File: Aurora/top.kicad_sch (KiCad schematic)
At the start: 5 parts, among them J4 Screw_Terminal_01x08, J5 Screw_Terminal_01x08, U10 ADS1115IDGS, U11 ADS1115IDGS, U9 MCP23017T-E_SO

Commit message: reorganization
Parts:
- removed J4, J5: Screw_Terminal_01x08, footprints7:CONN_1715789_PXC, symbol Connector:Screw_Terminal_01x08
- removed U9: MCP23017T-E_SO, MCP23017T_E_SO:SOIC127P1030X265-28N, symbol MCP23017T-E_SO:MCP23017T-E_SO
- added C51: 0.33uF, Capacitor_SMD:C_1206_3216Metric, symbol Device:C_Small
- added C52: 100nF, Capacitor_SMD:C_1206_3216Metric, symbol Device:C_Small
- added J19, J20: TSW-104-27-G-D, TSW_104_27_G_D:SAMTEC_TSW-104-27-G-D, symbol TSW-104-27-G-D:TSW-104-27-G-D
- added J21: XT60-M, XT60-M:AMASS_XT60-M, symbol XT60-M:XT60-M
- added U12: L7805, L7805:TO255P1020X450X2000-3, symbol Regulator_Linear:L7805
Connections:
- net 5V: now also C52.1, J19.02, U12.3 (OUT)
- net ADC1_SCL: now also J19.04
- net ADC1_SDA: now also J19.03
- net ADC2_SCL: now also J19.06
- net ADC2_SDA: now also J19.05
- net GND: now also C51.2, C52.2, J19.08, J21.N (NEG), U12.2 (GND)
- new net 7.4V: C51.1, J20.01, J21.P (POS), U12.1 (IN)
- new net HDR_GPIO1: J20.02
- new net HDR_GPIO2: J20.03
- new net HDR_GPIO3: J20.04
- new net HDR_GPIO4: J20.05
- new net HDR_GPIO5: J20.06
- new net HDR_GPIO6: J20.07
- new net HDR_GPIO7: J20.08
- new net HDR_GPIO8: J19.01
- new net PYRO2: J19.07
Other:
- note added: "male Header Pins from bottom board"
- note removed: "16 I/O I2C Expander"

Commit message: Add files via upload
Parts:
- added C53, C58: 16PX10000MEFC16X31.5, CAP_PK/PZ_16X31P5_RUB, symbol 2025-11-18_06-04-35:16PX10000MEFC16X31.5
- added D1, D8: LED, LED_SMD:LED_Cree-PLCC4_5x5mm_CW, symbol Device:LED
- added D7: WS2812B-2020, LED_SMD:LED_WS2812B-2020_PLCC4_2.0x2.0mm, symbol LED:WS2812B-2020
- added J17: Screw_Terminal_01x02, footprints5:CONN_1729128_PXC, symbol Connector:Screw_Terminal_01x02
- added J18: Screw_Terminal_01x04, footprints6:CONN_1715747_PXC, symbol Connector:Screw_Terminal_01x04
- added J26, J27: Screw_Terminal_01x08, footprints7:CONN_1715789_PXC, symbol Connector:Screw_Terminal_01x08
- added J28, J29, J30, J31, J32, J37, J38: Screw_Terminal_01x03, symbol Connector:Screw_Terminal_01x03
- added J39: TSW-104-27-G-D, TSW_104_27_G_D:SAMTEC_TSW-104-27-G-D, symbol TSW-104-27-G-D:TSW-104-27-G-D
- added J40: XT60-M, XT60-M:AMASS_XT60-M, symbol XT60-M:XT60-M
- added R17: 10k, Resistor_SMD:R_1206_3216Metric, symbol Device:R_Small
- added R20: 20k, Resistor_SMD:R_1206_3216Metric, symbol Device:R_Small
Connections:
- net 5V: now also J27.1 (Pin_1), J27.2 (Pin_2), J27.3 (Pin_3), J27.4 (Pin_4), J27.5 (Pin_5), J27.6 (Pin_6), J27.7 (Pin_7), J27.8 (Pin_8)
- net 7.4V: now also C53.1, J28.2 (Pin_2), J29.2 (Pin_2), J30.2 (Pin_2), J31.2 (Pin_2), J32.2 (Pin_2), J37.2 (Pin_2), J38.2 (Pin_2), R17.1
- net ADC1_IN2: now also J17.1 (Pin_1)
- net ADC1_IN3: now also J17.2 (Pin_2)
- net ADC2_IN0: now also J18.1 (Pin_1)
- net ADC2_IN1: now also J18.2 (Pin_2)
- net ADC2_IN2: now also J18.3 (Pin_3)
- net ADC2_IN3: now also J18.4 (Pin_4)
- net GND: now also C53.2, C58.2, D1.1 (K), D7.2 (VSS), D8.1 (K), J26.1 (Pin_1), J26.2 (Pin_2), J26.3 (Pin_3), J26.4 (Pin_4), J26.5 (Pin_5), J26.6 (Pin_6), J26.7 (Pin_7), J26.8 (Pin_8), J28.3 (Pin_3), J29.3 (Pin_3), J30.3 (Pin_3), J31.3 (Pin_3), J32.3 (Pin_3), J37.3 (Pin_3), J38.3 (Pin_3), J40.N (NEG)
- net HDR_GPIO1: now also J39.01; no longer J20.02
- net HDR_GPIO2: now also J39.02; no longer J20.03
- net HDR_GPIO3: now also J39.03; no longer J20.04
- net HDR_GPIO4: now also J39.04; no longer J20.05
- net HDR_GPIO5: now also D7.3 (DIN), J39.05; no longer J20.06
- net ADC1_IN0 renamed PYRO1_CONT
- net ADC1_IN1 renamed PYRO2_CONT
- net HDR_GPIO6 renamed SERVO6
- net SERVO6: now also J37.1 (Pin_1), J38.1 (Pin_1)
- net HDR_GPIO7 renamed SERVO7
- net HDR_GPIO8 renamed PYRO1_GPIO
- net PYRO2 renamed PYRO2_GPIO
- new net: D1.2 (A), R17.2
- new net: D8.2 (A), R20.2
- new net 12V: J40.P (POS), R20.1
- new net 12v: C58.1
- new net 3V3: D7.4 (VDD)
- new net SERVO1: J20.02, J28.1 (Pin_1)
- new net SERVO2: J20.03, J29.1 (Pin_1)
- new net SERVO3: J20.04, J30.1 (Pin_1)
- new net SERVO4: J20.05, J31.1 (Pin_1)
- new net SERVO5: J20.06, J32.1 (Pin_1)
- new net SLN_1: J39.07
- new net SLN_2: J39.08
- new net SPKG: J39.06
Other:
- note added: "10,000uF"
- note added: "ADC"
- note added: "Add redundant mosfets for powering solenoid"
- note added: "Blue LED"
- note added: "Check works with 3.3v logic (may need 5v booster)"
- note added: "Green LED"
- note added: "MISC"
- note added: "PYRO"
- note added: "Peripherals from bottom"
- note added: "Power Top"
- note added: "Servos"
- note added: "Solenoid"
- note added: "Spark Plug"
- moved on the sheet: C51, C52, J19, J20, J21, U10, U11, U12

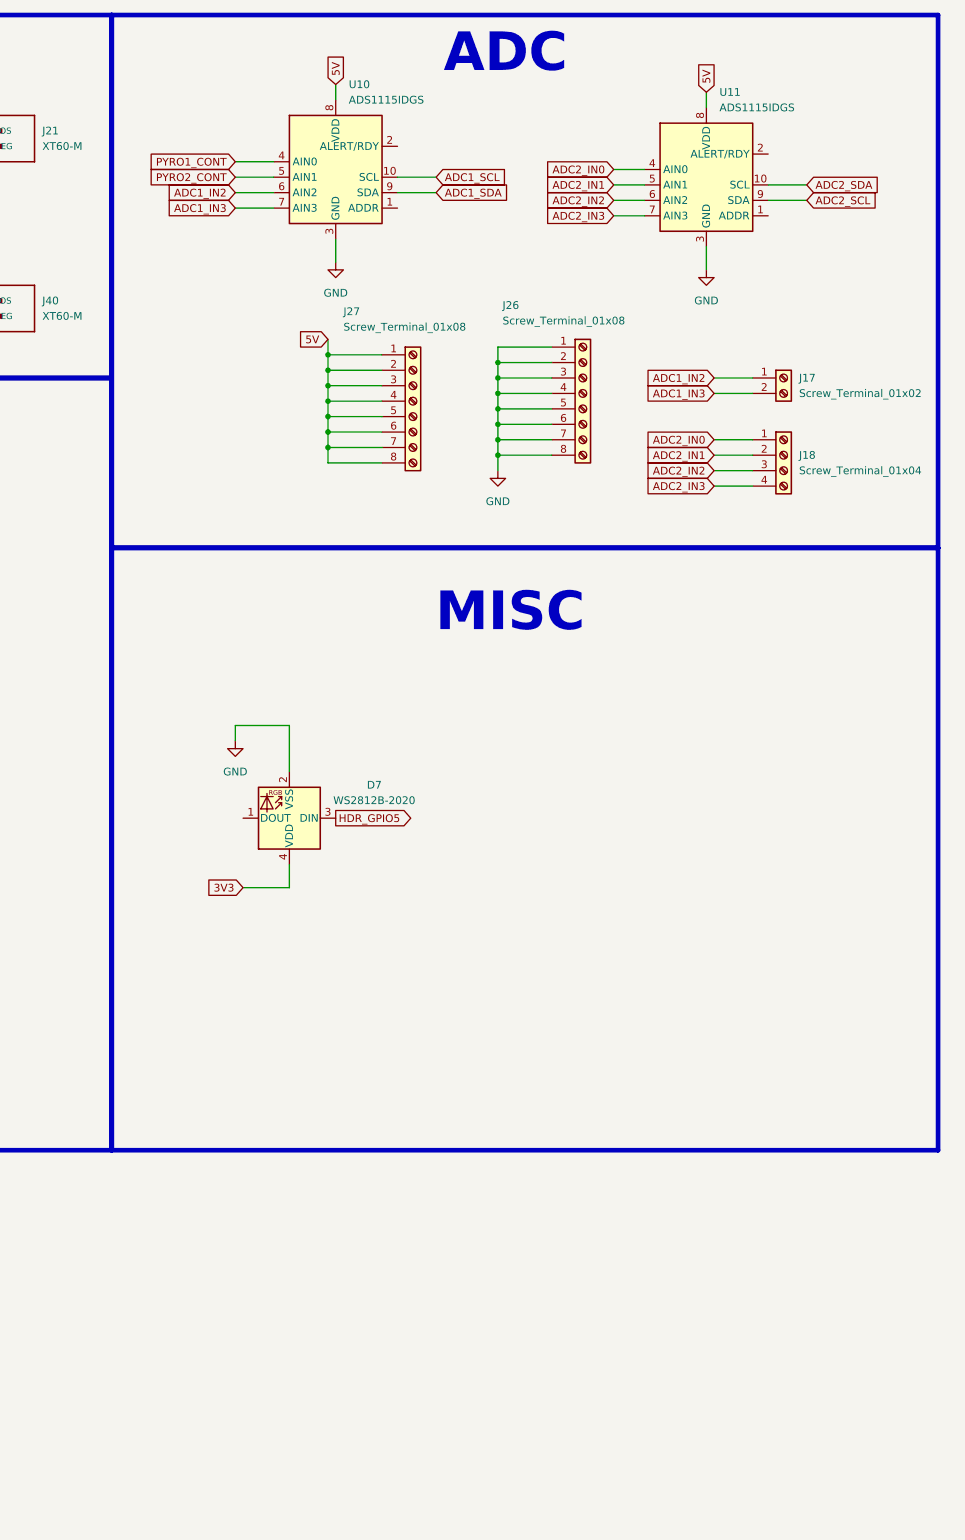
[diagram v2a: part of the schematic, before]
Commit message: 3rd ADC
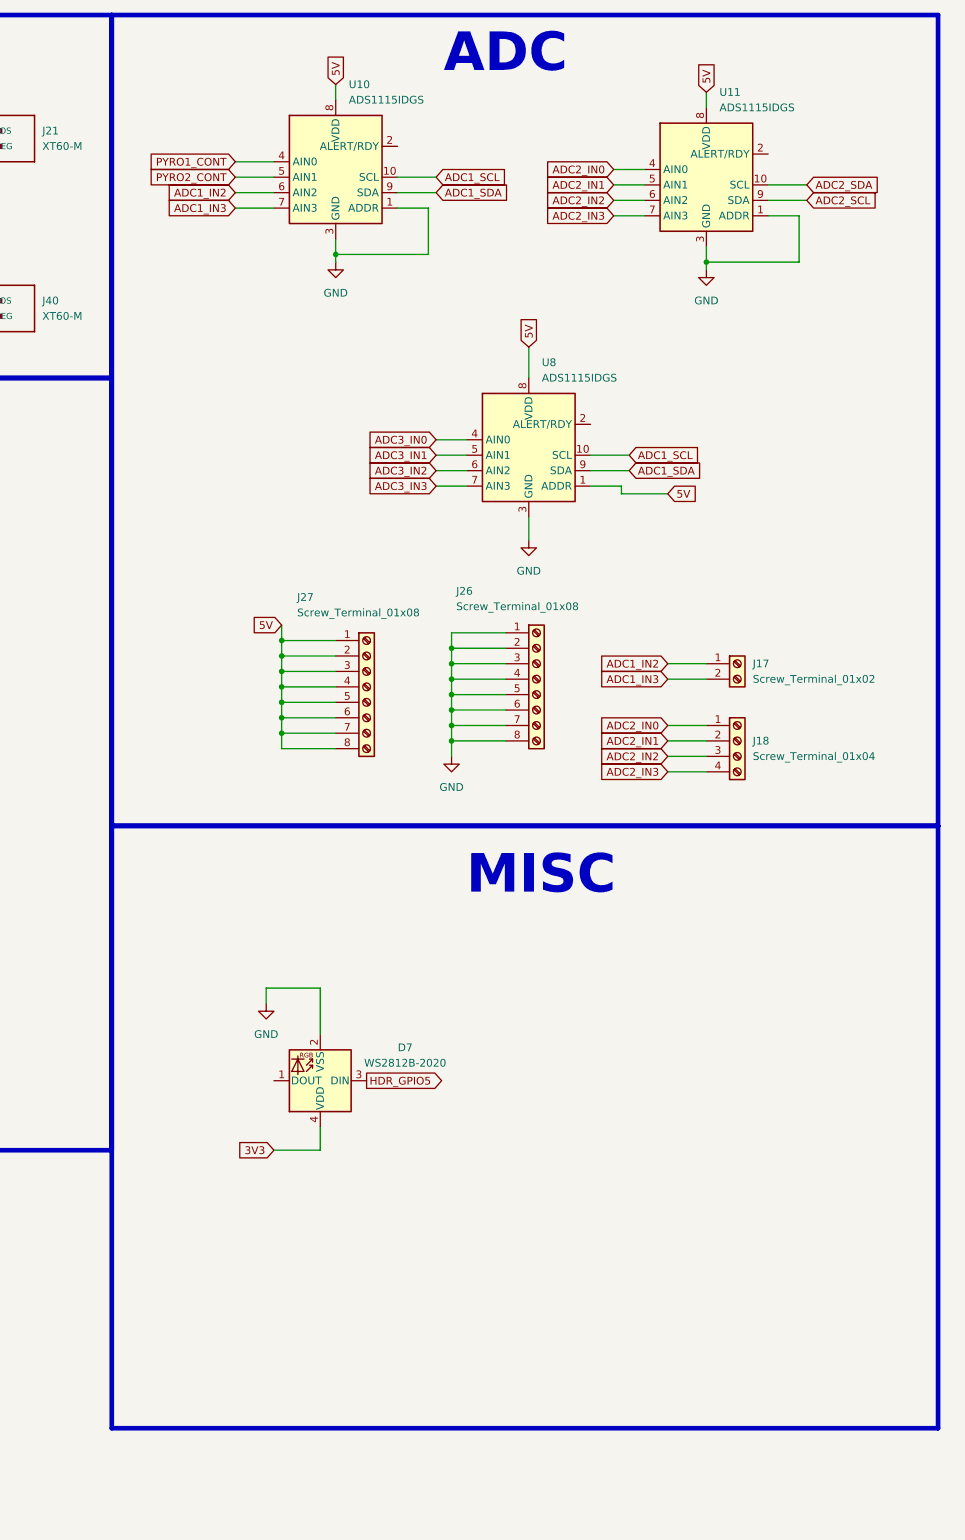
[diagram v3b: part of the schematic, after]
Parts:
- added U8: ADS1115IDGS, Package_SO:TSSOP-10_3x3mm_P0.5mm, symbol Analog_ADC:ADS1115IDGS
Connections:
- net 5V: now also U8.1 (ADDR), U8.8 (VDD)
- net ADC1_SCL: now also U8.10 (SCL)
- net ADC1_SDA: now also U8.9 (SDA)
- net GND: now also U10.1 (ADDR), U11.1 (ADDR), U8.3 (GND)
- new net ADC3_IN0: U8.4 (AIN0)
- new net ADC3_IN1: U8.5 (AIN1)
- new net ADC3_IN2: U8.6 (AIN2)
- new net ADC3_IN3: U8.7 (AIN3)
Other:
- moved on the sheet: D7, J17, J18, J26, J27
